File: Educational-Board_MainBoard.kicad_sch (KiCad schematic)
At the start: 0 parts

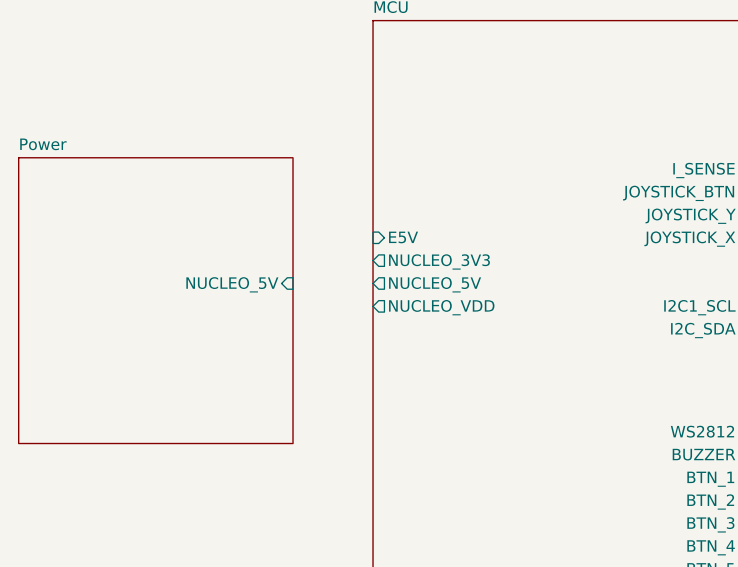
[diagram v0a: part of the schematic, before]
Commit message: fixed #1 , added protection circuit 5V selector jumper
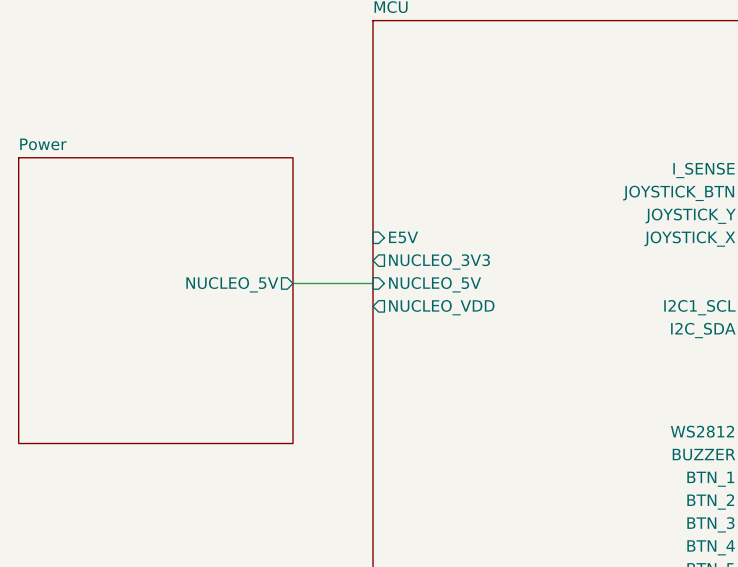
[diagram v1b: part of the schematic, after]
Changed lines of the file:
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@@
 	(title_block
 		(title "Think Embedded dev Board")
-		(date "2026-01-11")
+		(date "2026-03-12")
 		(rev "1.0")
 		(company "Filippo Castellan, Alan Masutti")
@@
 		(pts
 			(xy 153.67 82.55) (xy 173.99 82.55)
+		)
+		(stroke
+			(width 0)
+			(type default)
+		)
+	)
+	(wire
+		(pts
+			(xy 102.87 60.96) (xy 111.76 60.96)
 		)
 		(stroke
@@
 			)
 		)
-		(pin "NUCLEO_5V" input
+		(pin "NUCLEO_5V" output
 			(at 102.87 60.96 0)
 			(effects
@@
 			)
 		)
-		(pin "NUCLEO_5V" output
-			(at 111.76 60.96 180)
-			(effects
-				(font
-					(size 1.27 1.27)
-				)
-				(justify left)
-			)
-		)
 		(pin "NUCLEO_VDD" output
 			(at 111.76 63.5 180)
@@
 			)
 		)
+		(pin "NUCLEO_5V" input
+			(at 111.76 60.96 180)
+			(effects
+				(font
+					(size 1.27 1.27)
+				)
+				(justify left)
+			)
+		)
